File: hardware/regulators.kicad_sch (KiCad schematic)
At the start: 25 parts, among them U10 TPS54202DDC, U11 LM5163DDA, U12 AMS1117-3.3

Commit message: Fix LCSC part number on regulator output caps
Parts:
- C43, C44: LCSC C476766 -> C45783
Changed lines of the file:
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@@
 			)
 		)
-		(property "LCSC" "C476766"
+		(property "LCSC" "C45783"
 			(at 161.29 135.89 0)
 			(effects
@@
 			)
 		)
-		(property "LCSC" "C476766"
+		(property "LCSC" "C45783"
 			(at 152.4 135.89 0)
 			(effects

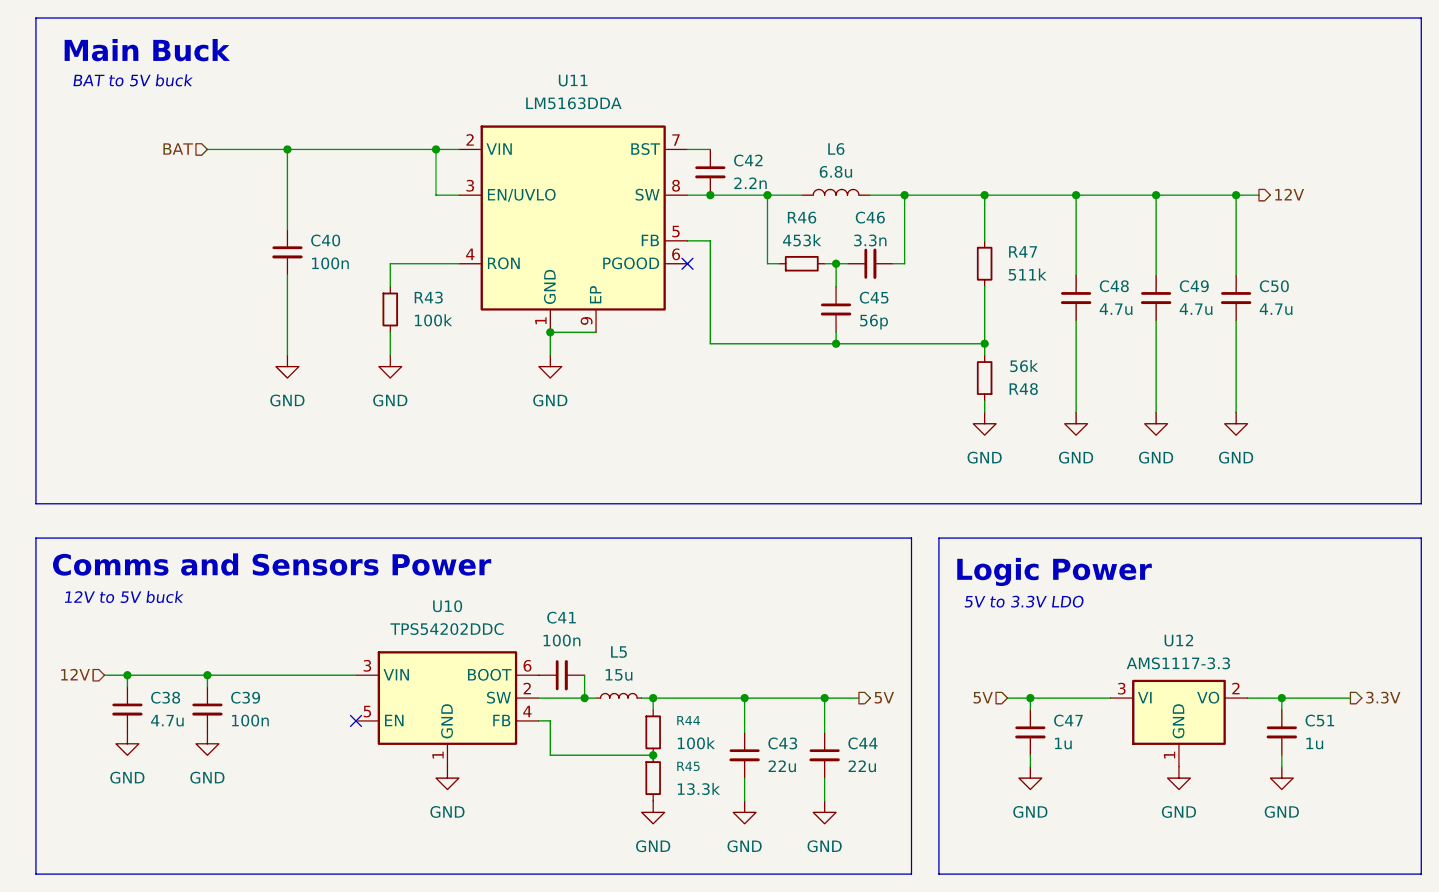
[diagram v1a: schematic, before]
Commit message: TVS and eletrolythic cap
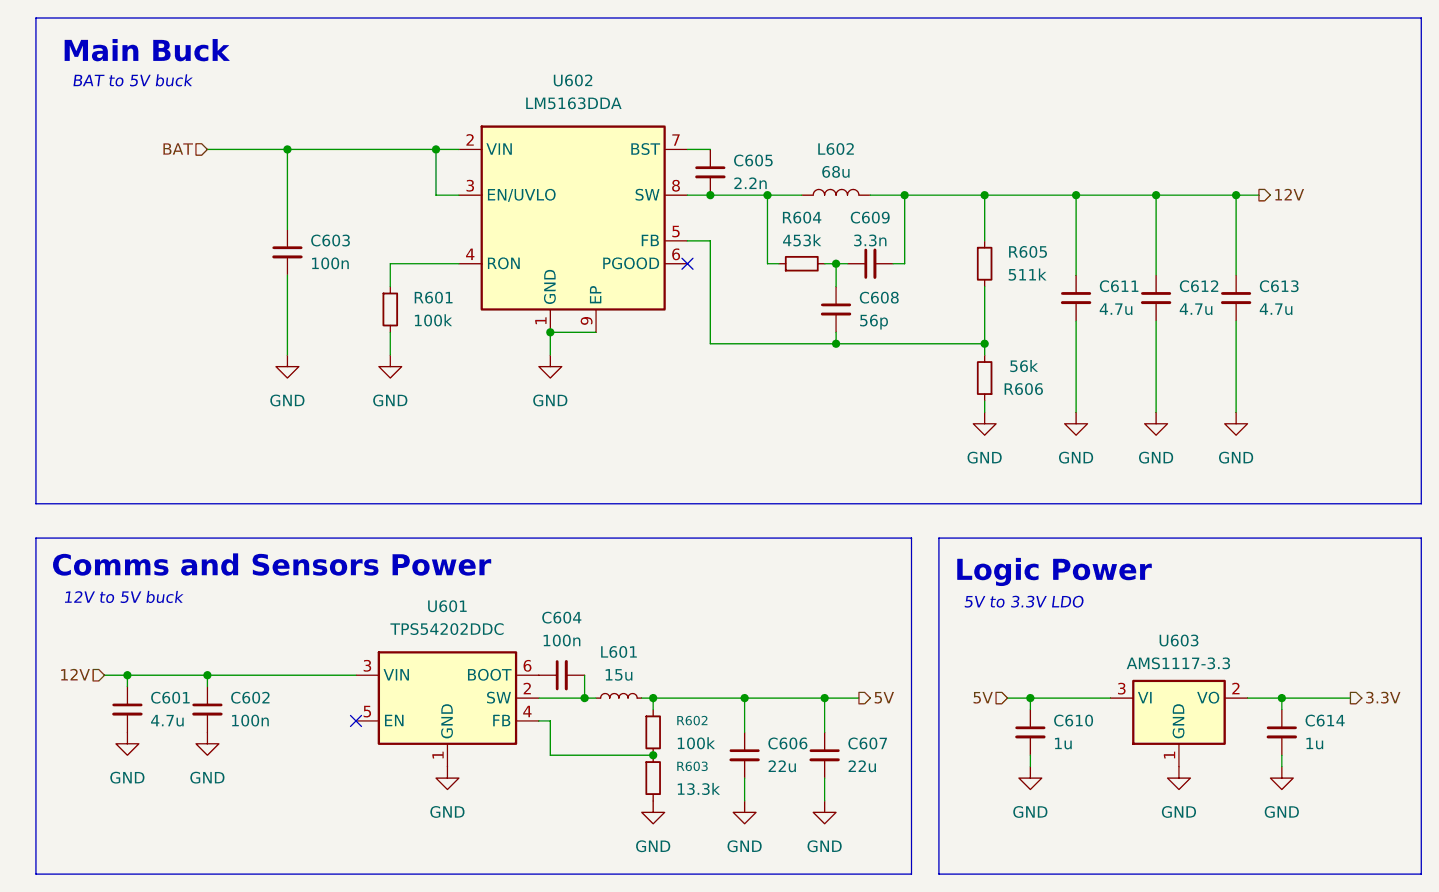
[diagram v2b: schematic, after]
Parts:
- L602: renamed from L6; value 6.8u -> 68u
- renumbered C38 to C601, C39 to C602, C40 to C603, C41 to C604, C42 to C605, C43 to C606, C44 to C607, C45 to C608, C46 to C609, C47 to C610, C48 to C611, C49 to C612, C50 to C613, C51 to C614, L5 to L601, R43 to R601, R44 to R602, R45 to R603, R46 to R604, R47 to R605, R48 to R606, U10 to U601, U11 to U602, U12 to U603

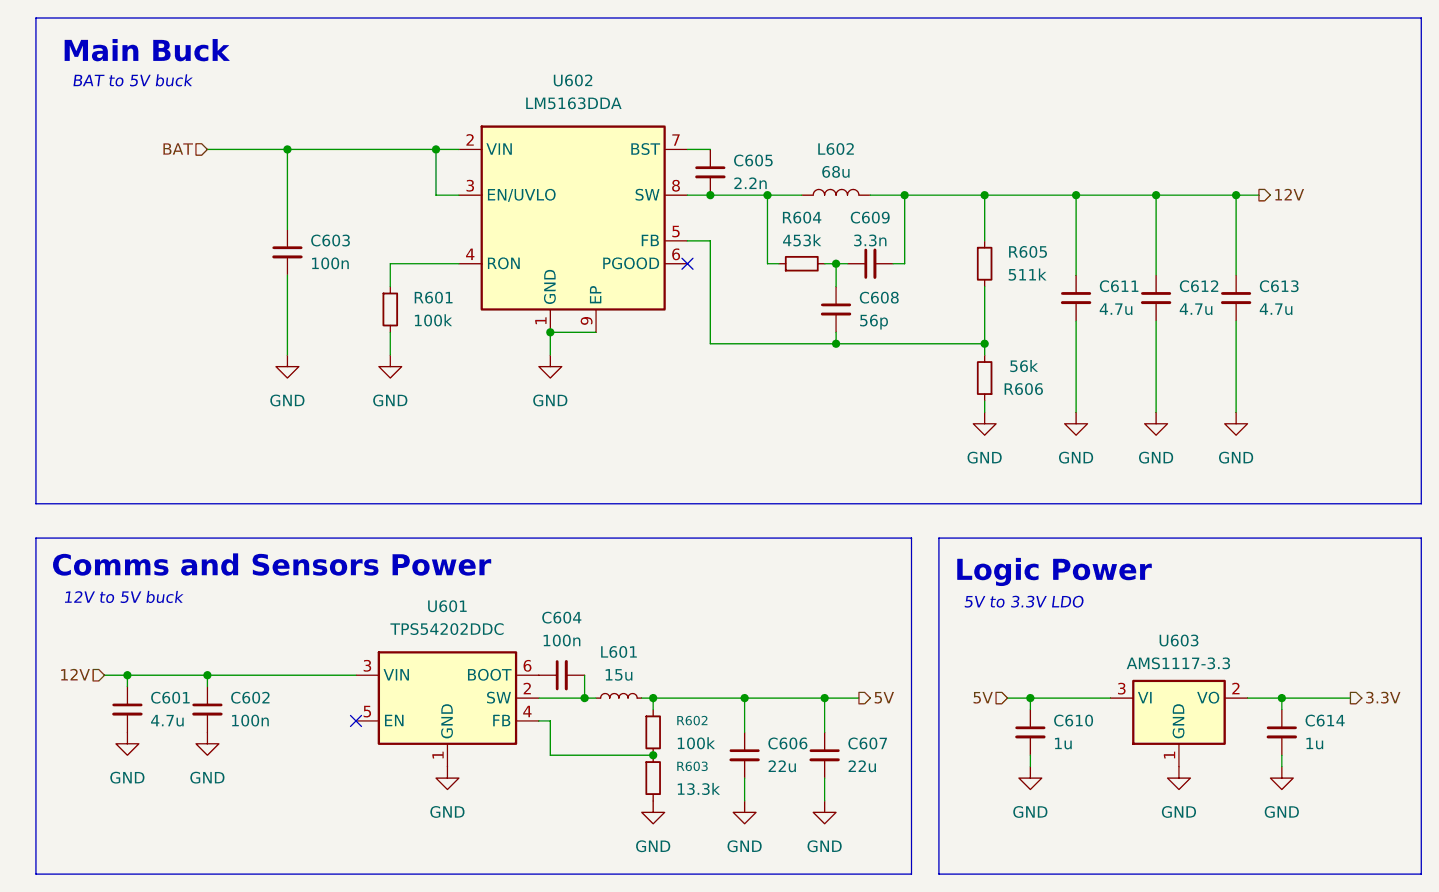
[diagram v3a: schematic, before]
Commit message: Reduce board size
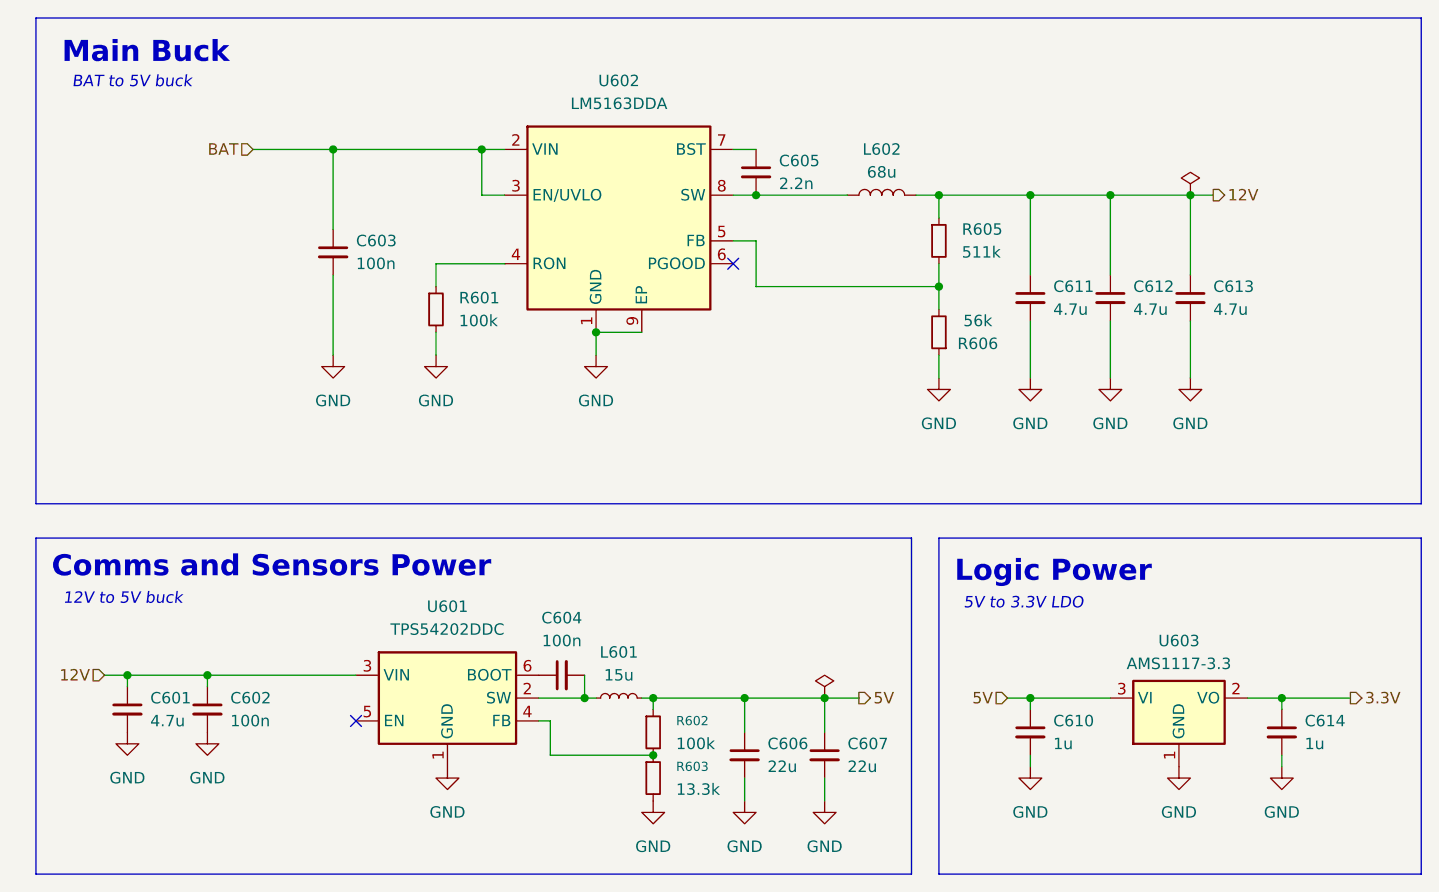
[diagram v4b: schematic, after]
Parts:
- removed C608: 56p, Capacitor_SMD:C_0603_1608Metric, symbol Device:C_Small
- removed C609: 3.3n, Capacitor_SMD:C_0603_1608Metric, symbol Device:C_Small
- removed R604: 453k, Resistor_SMD:R_0603_1608Metric, symbol Device:R_Small
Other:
- moved on the sheet: C603, C605, C611, C612, C613, L602, R601, R605, R606, U602
